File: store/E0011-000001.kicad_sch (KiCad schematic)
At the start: 126 parts, among them J1 Header A 2x12, J10 U3 U4 1-Wire, J11 RT2 lead, J12 SF1 flow switch, J13 E6 valve, J14 expansion, J15 RT3 RT4 leads, J2 Header B 2x10, J3 +24V in, J4 E1 to E0012, J5 fan E2, J6 E0012 sensing, J7 E3 subcooler, J8 E4 reheater, J9 fan E5, Q1 2N7002, Q2 2N7002, Q3 TBD, Q4 TBD, U10 M24C64, U11 SN74LVC08AD, U5 DRV8262DDW, U6 DRV8262DDW, U7 MCP6567, U8 MCP6569, U9 PCA9685PW

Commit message: Schematic: E0011 blocks drawn, GPIO_6 and GPIO_7
The Header B spare inputs take their carrier names. J1 and J2 take the
header symbol values. The sheet is divided into bordered, labelled
blocks with the carrier header at the top right. A stub wire, its
junction and a no-connect flag, all reaching nothing, are removed.

Signed-off-by: IIchukissII <133657307+IIchukissII@users.noreply.github.com>
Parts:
- J1: value Header A 2x12 -> Sensor_Header_A
- J2: value Header B 2x10 -> Sensor_Header_B
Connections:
- net STRAP_1 renamed GPIO_6
- net STRAP_2 renamed GPIO_7
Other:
- note added: "+24 V actuator section (SP0010)"
- note added: "CO2 branch E6 (not populated)"
- note added: "Carrier Header"
- note added: "Drive expansion"
- note added: "Driver enable chain"
- note added: "E1 main stack, single H-bridge"
- note added: "E3 subcooler and E4 reheater, dual H-bridge"
- note added: "Element outputs"
- note added: "Field leads"
- note added: "Hardware interlocks T2-T5"
- note added: "Logic decoupling"
- note added: "Module-ID (0x80)"
- note added: "Signal reserve"
- note added: "Spare thermistor channels"
- note added: "Tract fans E2 E5 (SP0008)"
- note removed: "+24 V ACTUATOR SECTION SP0010"
- note removed: "CARRIER INTERFACE"
- note removed: "CO2 BRANCH E6 NOT POPULATED"
- note removed: "DRIVER ENABLE CHAIN"
- note removed: "E1 MAIN THERMOELECTRIC STACK single H-bridge"
- note removed: "E3 SUBCOOLER E4 REHEATER dual H-bridge"
- note removed: "ELEMENT OUTPUTS"
- note removed: "FIELD LEADS"
- note removed: "HARDWARE INTERLOCKS T2 T3 T4 T5"
- note removed: "LOGIC DECOUPLING"
- note removed: "MODULE CLASS ID 0x80"
- note removed: "MODULE-LOCAL DRIVE EXPANSION"
- note removed: "SIGNAL RESERVE"
- note removed: "SPARE THERMISTOR CHANNELS"
- note removed: "TRACT FANS E2 E5 SP0008"
- moved on the sheet: C10, C11, C12, C13, C14, C15, C16, C17, C18, C19, C20, C21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

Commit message: Store: DRV8262 footprint with 0.3 mm thermal vias
- industrygrow.pretty: HTSSOP-44 ThermalVias footprint derived from the KiCad library, via drill changed.
- industrygrow.kicad_sym: DRV8262DDW default footprint set to it.
- E0011-000001.kicad_sch: U5, U6 footprint set to it.
- REUSE.toml, LICENSE.md: the footprint annotated CC-BY-SA-4.0, KiCad Libraries Team.

Signed-off-by: IIchukissII <133657307+IIchukissII@users.noreply.github.com>
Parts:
- U5, U6: footprint Package_SO:HTSSOP-44-1EP_6.1x14mm_P0.635mm_EP5.2x14mm_Mask4.31x8.26mm_ThermalVias -> industrygrow:HTSSOP-44-1EP_6.1x14mm_P0.635mm_EP5.2x14mm_Mask4.31x8.26mm_ThermalVias_Drill0.3mm
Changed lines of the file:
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@@
 			)
 		)
-		(property "Footprint" "Package_SO:HTSSOP-44-1EP_6.1x14mm_P0.635mm_EP5.2x14mm_Mask4.31x8.26mm_ThermalVias"
+		(property "Footprint" "industrygrow:HTSSOP-44-1EP_6.1x14mm_P0.635mm_EP5.2x14mm_Mask4.31x8.26mm_ThermalVias_Drill0.3mm"
 			(at 327.66 68.7 0)
 			(hide yes)
@@
 			)
 		)
-		(property "Footprint" "Package_SO:HTSSOP-44-1EP_6.1x14mm_P0.635mm_EP5.2x14mm_Mask4.31x8.26mm_ThermalVias"
+		(property "Footprint" "industrygrow:HTSSOP-44-1EP_6.1x14mm_P0.635mm_EP5.2x14mm_Mask4.31x8.26mm_ThermalVias_Drill0.3mm"
 			(at 327.66 256.66 0)
 			(hide yes)

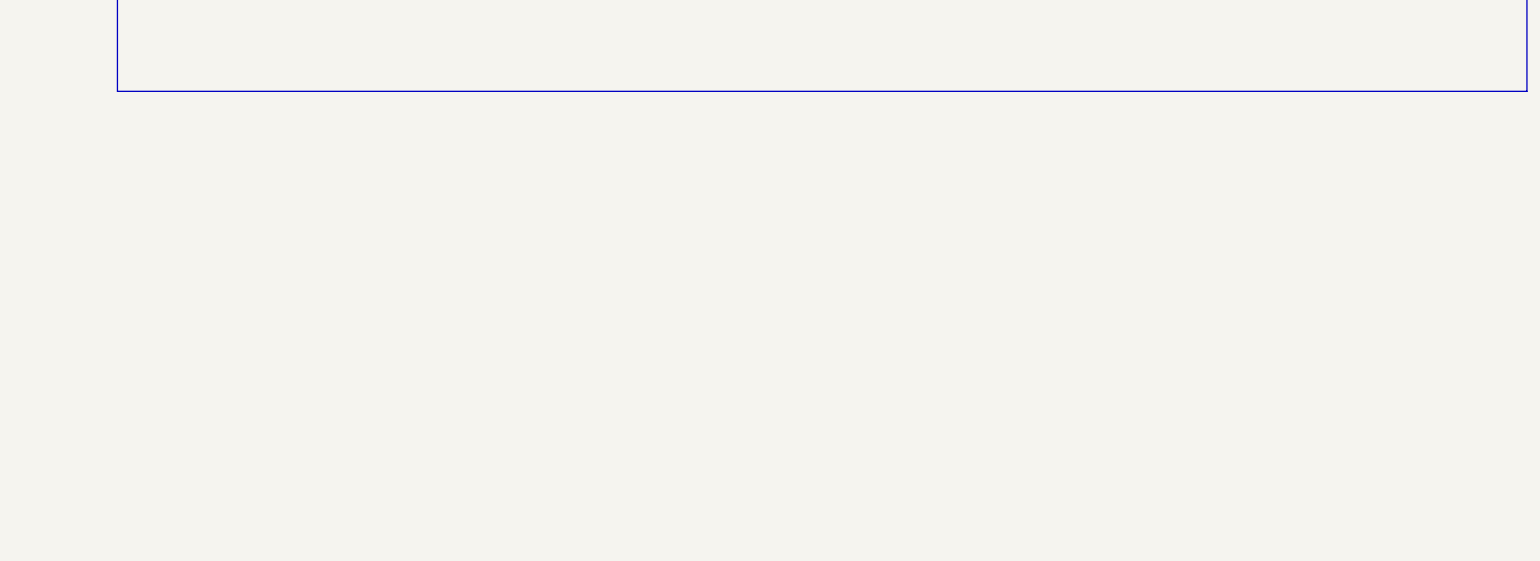
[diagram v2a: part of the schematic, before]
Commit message: E0011: test points
- E0011-000001.kicad_sch: Test points block, TP1–TP20, one per net the spec §11 checks probe.

Signed-off-by: IIchukissII <133657307+IIchukissII@users.noreply.github.com>
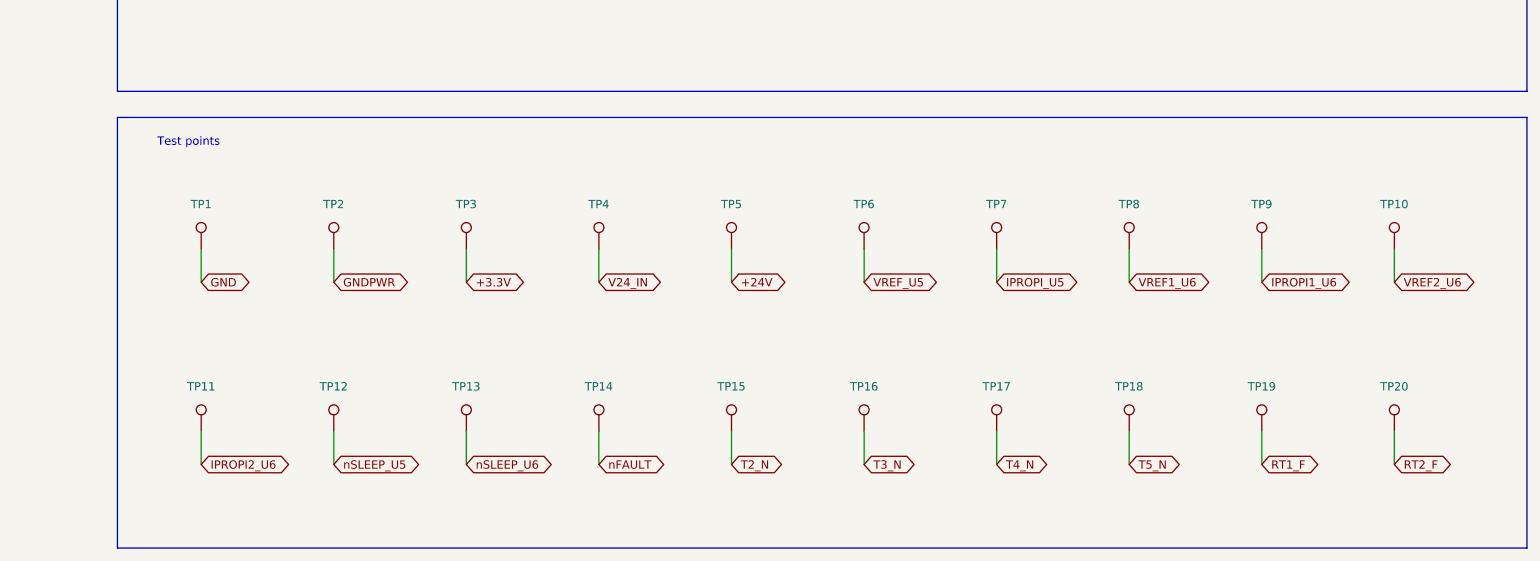
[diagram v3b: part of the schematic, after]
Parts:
- added TP1, TP10, TP11, TP12, TP13, TP14, TP15, TP16, TP17, TP18, TP19, TP2, TP20, TP3, TP4, TP5, TP6, TP7, TP8, TP9: TestPoint, TestPoint:TestPoint_Pad_D1.5mm, symbol Connector:TestPoint
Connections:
- net +24V: now also TP5.1
- net +3.3V: now also TP3.1
- net GND: now also TP1.1
- net GNDPWR: now also TP2.1
- net IPROPI1_U6: now also TP9.1
- net IPROPI2_U6: now also TP11.1
- net IPROPI_U5: now also TP7.1
- net RT1_F: now also TP19.1
- net RT2_F: now also TP20.1
- net T2_N: now also TP15.1
- net T3_N: now also TP16.1
- net T4_N: now also TP17.1
- net T5_N: now also TP18.1
- net V24_IN: now also TP4.1
- net VREF1_U6: now also TP8.1
- net VREF2_U6: now also TP10.1
- net VREF_U5: now also TP6.1
- net nFAULT: now also TP14.1
- net nSLEEP_U5: now also TP12.1
- net nSLEEP_U6: now also TP13.1
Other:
- note added: "Test points"

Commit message: E0011: latching connectors on the field leads
The seven sensing and fan leads carry Micro-Fit 3.0 horizontal headers, whose
latch and through-hole tails retain the mating connector. Every 24 V lead now
leaves the board on the terminal edge and the opposite edge carries sensing
only. Circuit counts, net membership and the unconnected count are unchanged.

Signed-off-by: IIchukissII <133657307+IIchukissII@users.noreply.github.com>
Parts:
- J10: footprint Connector_PinHeader_2.54mm:PinHeader_1x03_P2.54mm_Vertical -> Connector_Molex:Molex_Micro-Fit_3.0_43650-0300_1x03_P3.00mm_Horizontal
- J11, J12: footprint Connector_PinHeader_2.54mm:PinHeader_1x02_P2.54mm_Vertical -> Connector_Molex:Molex_Micro-Fit_3.0_43650-0200_1x02_P3.00mm_Horizontal
- J15, J5, J9: footprint Connector_PinHeader_2.54mm:PinHeader_1x04_P2.54mm_Vertical -> Connector_Molex:Molex_Micro-Fit_3.0_43650-0400_1x04_P3.00mm_Horizontal
- J6: footprint Connector_PinHeader_2.54mm:PinHeader_1x05_P2.54mm_Vertical -> Connector_Molex:Molex_Micro-Fit_3.0_43650-0500_1x05_P3.00mm_Horizontal
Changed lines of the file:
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@@
 			)
 		)
-		(property "Footprint" "Connector_PinHeader_2.54mm:PinHeader_1x03_P2.54mm_Vertical"
+		(property "Footprint" "Connector_Molex:Molex_Micro-Fit_3.0_43650-0300_1x03_P3.00mm_Horizontal"
 			(at 63.5 61.08 0)
 			(hide yes)
@@
 			)
 		)
-		(property "Footprint" "Connector_PinHeader_2.54mm:PinHeader_1x02_P2.54mm_Vertical"
+		(property "Footprint" "Connector_Molex:Molex_Micro-Fit_3.0_43650-0200_1x02_P3.00mm_Horizontal"
 			(at 63.5 101.72 0)
 			(hide yes)
@@
 			)
 		)
-		(property "Footprint" "Connector_PinHeader_2.54mm:PinHeader_1x02_P2.54mm_Vertical"
+		(property "Footprint" "Connector_Molex:Molex_Micro-Fit_3.0_43650-0200_1x02_P3.00mm_Horizontal"
 			(at 63.5 82.67 0)
 			(hide yes)
@@
 			)
 		)
-		(property "Footprint" "Connector_PinHeader_2.54mm:PinHeader_1x04_P2.54mm_Vertical"
+		(property "Footprint" "Connector_Molex:Molex_Micro-Fit_3.0_43650-0400_1x04_P3.00mm_Horizontal"
 			(at 500.38 273.17 0)
 			(hide yes)
@@
 			)
 		)
-		(property "Footprint" "Connector_PinHeader_2.54mm:PinHeader_1x04_P2.54mm_Vertical"
+		(property "Footprint" "Connector_Molex:Molex_Micro-Fit_3.0_43650-0400_1x04_P3.00mm_Horizontal"
 			(at 500.38 235.07 0)
 			(hide yes)
@@
 			)
 		)
-		(property "Footprint" "Connector_PinHeader_2.54mm:PinHeader_1x04_P2.54mm_Vertical"
+		(property "Footprint" "Connector_Molex:Molex_Micro-Fit_3.0_43650-0400_1x04_P3.00mm_Horizontal"
 			(at 670.56 350.64 0)
 			(hide yes)
@@
 			)
 		)
-		(property "Footprint" "Connector_PinHeader_2.54mm:PinHeader_1x05_P2.54mm_Vertical"
+		(property "Footprint" "Connector_Molex:Molex_Micro-Fit_3.0_43650-0500_1x05_P3.00mm_Horizontal"
 			(at 63.5 30.6 0)
 			(hide yes)

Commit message: E0011: control-band passives on 0603, support parts moved, inner planes added
Signed-off-by: IIchukissII <133657307+IIchukissII@users.noreply.github.com>
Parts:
- C11: footprint Capacitor_SMD:C_0805_2012Metric -> Capacitor_SMD:C_0603_1608Metric
- R29, R30, R31, R32, R33, R34, R35, R36, R37, R38, R39, R40, R41, R42: footprint Resistor_SMD:R_0805_2012Metric -> Resistor_SMD:R_0603_1608Metric
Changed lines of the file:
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@@
 			)
 		)
-		(property "Footprint" "Resistor_SMD:R_0805_2012Metric"
+		(property "Footprint" "Resistor_SMD:R_0603_1608Metric"
 			(at 412.75 148.71 0)
 			(hide yes)
@@
 			)
 		)
-		(property "Footprint" "Resistor_SMD:R_0805_2012Metric"
+		(property "Footprint" "Resistor_SMD:R_0603_1608Metric"
 			(at 412.75 395.09 0)
 			(hide yes)
@@
 			)
 		)
-		(property "Footprint" "Capacitor_SMD:C_0805_2012Metric"
+		(property "Footprint" "Capacitor_SMD:C_0603_1608Metric"
 			(at 434.34 226.18 0)
 			(hide yes)
@@
 			)
 		)
-		(property "Footprint" "Resistor_SMD:R_0805_2012Metric"
+		(property "Footprint" "Resistor_SMD:R_0603_1608Metric"
 			(at 434.34 285.87 0)
 			(hide yes)
@@
 			)
 		)
-		(property "Footprint" "Resistor_SMD:R_0805_2012Metric"
+		(property "Footprint" "Resistor_SMD:R_0603_1608Metric"
 			(at 434.34 316.35 0)
 			(hide yes)
@@
 			)
 		)
-		(property "Footprint" "Resistor_SMD:R_0805_2012Metric"
+		(property "Footprint" "Resistor_SMD:R_0603_1608Metric"
 			(at 458.47 119.5 0)
 			(hide yes)
@@
 			)
 		)
-		(property "Footprint" "Resistor_SMD:R_0805_2012Metric"
+		(property "Footprint" "Resistor_SMD:R_0603_1608Metric"
 			(at 455.93 316.35 0)
 			(hide yes)
@@
 			)
 		)
-		(property "Footprint" "Resistor_SMD:R_0805_2012Metric"
+		(property "Footprint" "Resistor_SMD:R_0603_1608Metric"
 			(at 412.75 181.73 0)
 			(hide yes)
@@
 			)
 		)
-		(property "Footprint" "Resistor_SMD:R_0805_2012Metric"
+		(property "Footprint" "Resistor_SMD:R_0603_1608Metric"
 			(at 455.93 345.56 0)
 			(hide yes)
@@
 			)
 		)
-		(property "Footprint" "Resistor_SMD:R_0805_2012Metric"
+		(property "Footprint" "Resistor_SMD:R_0603_1608Metric"
 			(at 434.34 119.5 0)
 			(hide yes)
@@
 			)
 		)
-		(property "Footprint" "Resistor_SMD:R_0805_2012Metric"
+		(property "Footprint" "Resistor_SMD:R_0603_1608Metric"
 			(at 412.75 345.56 0)
 			(hide yes)
@@
 			)
 		)
-		(property "Footprint" "Resistor_SMD:R_0805_2012Metric"
+		(property "Footprint" "Resistor_SMD:R_0603_1608Metric"
 			(at 412.75 316.35 0)
 			(hide yes)
@@
 			)
 		)
-		(property "Footprint" "Resistor_SMD:R_0805_2012Metric"
+		(property "Footprint" "Resistor_SMD:R_0603_1608Metric"
 			(at 412.75 407.79 0)
 			(hide yes)
@@
 			)
 		)
-		(property "Footprint" "Resistor_SMD:R_0805_2012Metric"
+		(property "Footprint" "Resistor_SMD:R_0603_1608Metric"
 			(at 434.34 395.09 0)
 			(hide yes)
@@
 			)
 		)
-		(property "Footprint" "Resistor_SMD:R_0805_2012Metric"
+		(property "Footprint" "Resistor_SMD:R_0603_1608Metric"
 			(at 434.34 148.71 0)
 			(hide yes)
